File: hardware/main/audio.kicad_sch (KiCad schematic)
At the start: 35 parts, among them J10 Haut-parleur, U2 PCM5122PW, U3 PAM8406DR, U4 ICS-43434

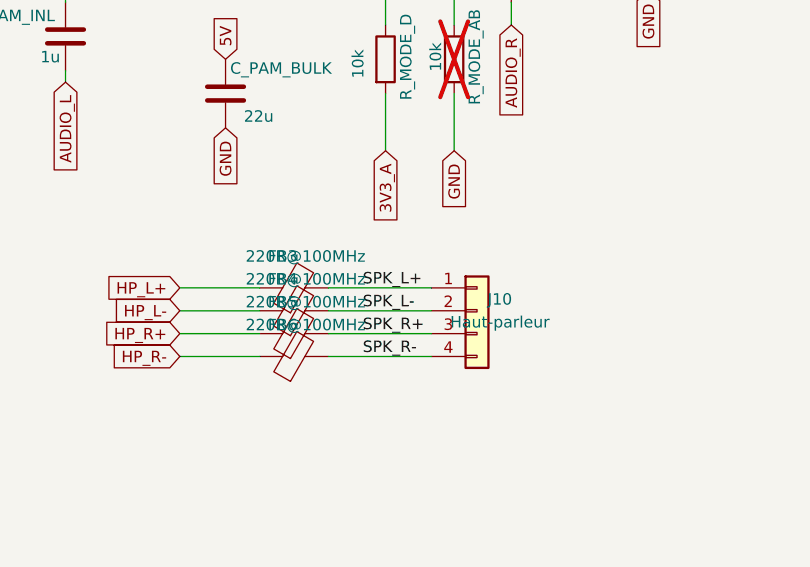
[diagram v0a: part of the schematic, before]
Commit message: hardware: pull-ups carte SD, resistances serie d'horloge, timer de charge
Trois points "important" de l'audit 2026-09-23, verifies un par un sur le
schema avant modification (tools/kicad_netlist.py).

H7 — carte SD : aucune pull-up sur J11. L'ESP-IDF les rend obligatoires
(sd_pullup_requirements.rst : « en mode SPI ou SD 1 bit, CMD et DAT0-DAT3
doivent etre tirees au plus par 10k, y compris les lignes non reliees a
l'hote »). Ajout de R15-R19 (10k) sur un rail 3V3_D commun, feuille connector.
DAT1 (J11.8) et DAT2 (J11.1) n'avaient aucun fil : nets nommes SD_DAT1/SD_DAT2.

H8 — horloges SPI : FB1/FB2 (ferrites 120R) remplacees par R13/R14 = 22 ohm
0603. Device:R et Device:FerriteBead ont leurs pins au meme endroit, donc les
fils et la connectivite sont inchanges. Une ferrite sur une horloge rapide
arrondit les fronts et viole les timings de la carte (ESP-IDF sdspi_share.rst,
AC loading) ; les yeux tournent a 40 MHz, 80 visees. Ajout de C6/C7, 10 pF vers
GND en DNP, comme provision jusqu'au test CEM.

H9 — charge LiPo : TMR etait cable directement a GND, c'est-a-dire timers de
securite desactives (bq24075 §6.1). Ajout de R_TMR 56k 1 % entre TMR et GND
-> t_MAXCHG = 10 x K_TMR x R_TMR = 5,6 a 9,3 h (K_TMR 36-60 s/kOhm), pour une
charge de ~4 h a 1 A sur 3000 mAh. Plage admissible datasheet : 18-72 kOhm.

A4 — ICS-43434 sans decouplage : CONSTAT ERRONE, aucune modification faite.
C3 (100 nF 0402, 3V3_A/GND) est deja place a cote de U4 et l'etait deja dans le
fichier du 23/09. Seule subsiste une contrainte de layout (au plus pres des
broches 5 et 3, sans via). Le rapport d'audit et la fiche datasheet sont annotes
en consequence.

tools/kicad_edit.py : helpers d'edition de schema (symboles, fils, labels,
jonctions, remplacement de composant a geometrie de pins identique).
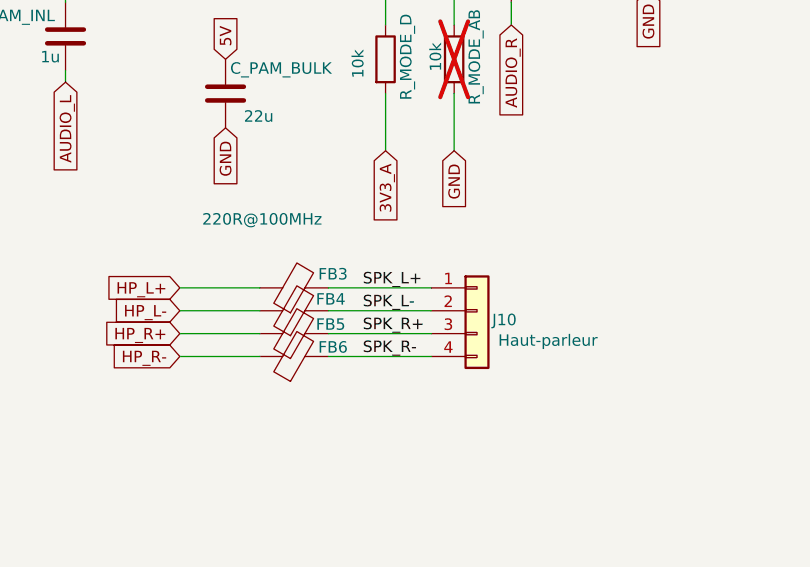
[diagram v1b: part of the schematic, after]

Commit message: hardware(power): corrections issues de l'ERC — jonction L1 et empreintes JST
Deux points remontes par l'ERC du 2026-09-27 (0 erreur, 148 warnings).

1. REGRESSION de ma part, corrigee : en isolant l'EN de U7 pour le net EN_SYS,
   j'avais aussi supprime la jonction (105.41, 111.76) en la croyant devenue
   inutile. Elle portait en realite une seconde derivation : VSYS -> L1,
   l'inductance du boost. Sans elle, KiCad signalait une extremite de fil non
   connectee — autrement dit le MT3608 n'etait plus alimente. Jonction
   retablie, L1.1 de nouveau sur VSYS (verifie par netlist).
   Lecon : une jonction peut porter plus de branches que celle qu'on retire ;
   verifier ce qui passe par le point avant de la supprimer.

2. Empreintes JST PH introuvables (J2, J9, J10) : le projet utilisait
   « ...1x02-P2.00mm... » alors que la bibliotheque KiCad nomme
   « ...1x02_P2.00mm... » (underscore et non tiret). Defaut preexistant sur J2
   et J9, que j'avais propage a J10 en copiant J9. Les trois noms sont
   corriges et verifies contre la bibliotheque officielle, de meme que toutes
   les empreintes ajoutees depuis (SOIC-8, SOT-23, L_0805, R_0603, R_0402,
   C_0402, JST_SH 1x02).
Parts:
- J10: footprint Connector_JST:JST_PH_B4B-PH-K_1x04-P2.00mm_Vertical -> Connector_JST:JST_PH_B4B-PH-K_1x04_P2.00mm_Vertical
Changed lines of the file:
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@@
 			)
 		)
-		(property "Footprint" "Connector_JST:JST_PH_B4B-PH-K_1x04-P2.00mm_Vertical"
+		(property "Footprint" "Connector_JST:JST_PH_B4B-PH-K_1x04_P2.00mm_Vertical"
 			(at 248.92 119.38 0)
 			(hide yes)

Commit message: hardware: 48 erreurs ERC traitees, 22 points de test poses, VBAT_SENSE retire de J8.5
Les rapports ERC precedents portaient « Report includes: Warnings » : les
erreurs en etaient exclues a l'export et le resume affichait « Errors 0 ».
Elles etaient donc presentes depuis le debut et je ne les ai pas vues — il faut
exporter avec les erreurs incluses.

48 erreurs, trois familles, toutes des faux positifs au sens electrique mais
qu'il faut declarer sinon l'ERC reste inexploitable :

1. power_pin_not_driven (14) : le projet n'utilise aucun symbole d'alimentation,
   les rails sont des global labels, et KiCad exige qu'un net « power input »
   soit pilote par une pin « power output ». Nine PWR_FLAG poses, un par rail
   (GND, VSYS, VBAT, VBAT-, 3V3_D, 3V3_A, 5V, 5V_BOOST, 5V_USB).
2. pin_not_connected (29) : broches volontairement libres — paires SuperSpeed et
   SBU de l'USB-C (design USB 2.0), UART0 et IO35-37 de l'ESP32 (reserves a la
   PSRAM octale), GPIO du PCM5122, interruptions de l'IMU, reserves de
   connecteurs, drains communs du FS8205. Marqueurs no_connect.
3. divers (5) : label GND orphelin hors page (122, 228.81 — la page fait
   210 mm de haut) supprime ; C1_AV/C2_DV/C3_CP renommes C_AVDD/C_DVDD/C_CPVDD
   (KiCad lit « C1_AV » comme un prefixe suivi de « 1_AV », donc non annote) ;
   OUT_11 du bq24075 passee en passive (les deux broches sont la meme sortie).

Points de test : les 22 valides sont poses, chacun relie par un fil court a un
global label (le routeur les placera ou ils sont accessibles). 22/22 verifies
sur leur net. Trois nets anonymes nommes au passage : BQ_ISET, BQ_CHG,
BOOST_FB. Avec les 4 existants, 26 points de test.

VBAT_SENSE retire de J8.5 : noeud ADC haute impedance (1M // 1M) sorti dans un
cable, sans usage cote face avant depuis que les analogiques passent par
l'ADS7830. Broche marquee non connectee.

CORRECTION D'OUTIL : tools/kicad_netlist.py comptait PWR_FLAG comme un nom de
net, ce qui faisait fusionner les neuf rails en un seul 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
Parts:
- added TP_AUDIOL, TP_I2SBCK, TP_I2SLRCK: TestPoint, TestPoint:TestPoint_Pad_D1.5mm, symbol Connector:TestPoint
- renumbered C1_AV to C_AVDD, C3_CP to C_CPVDD, C2_DV to C_DVDD
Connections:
- net AUDIO_L: now also TP_AUDIOL.1
- net I2S0_BCLK: now also TP_I2SBCK.1
- net I2S0_LRCK: now also TP_I2SLRCK.1
- no-connect marks 0 -> 4

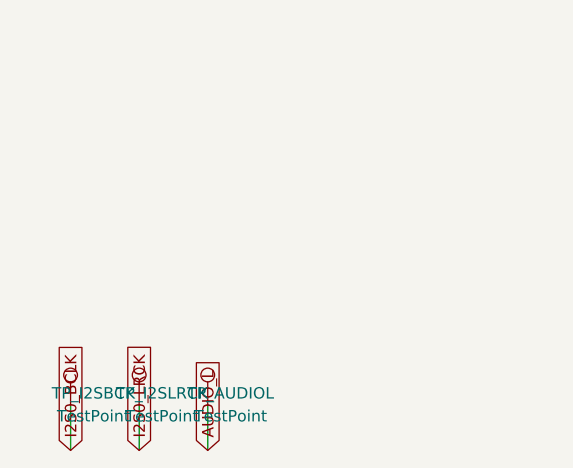
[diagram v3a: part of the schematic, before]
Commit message: datasheets: ATtiny1616, reference documentaire non inventee
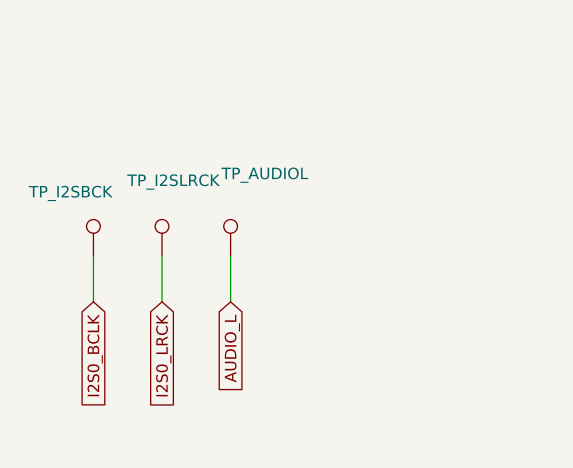
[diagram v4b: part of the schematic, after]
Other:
- moved on the sheet: TP_AUDIOL, TP_I2SBCK, TP_I2SLRCK
